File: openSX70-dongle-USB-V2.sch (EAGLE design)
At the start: 29 parts, among them J1 687106183722, J2 SJ-3523-SMT-TR, U1 FT232RLSSOP

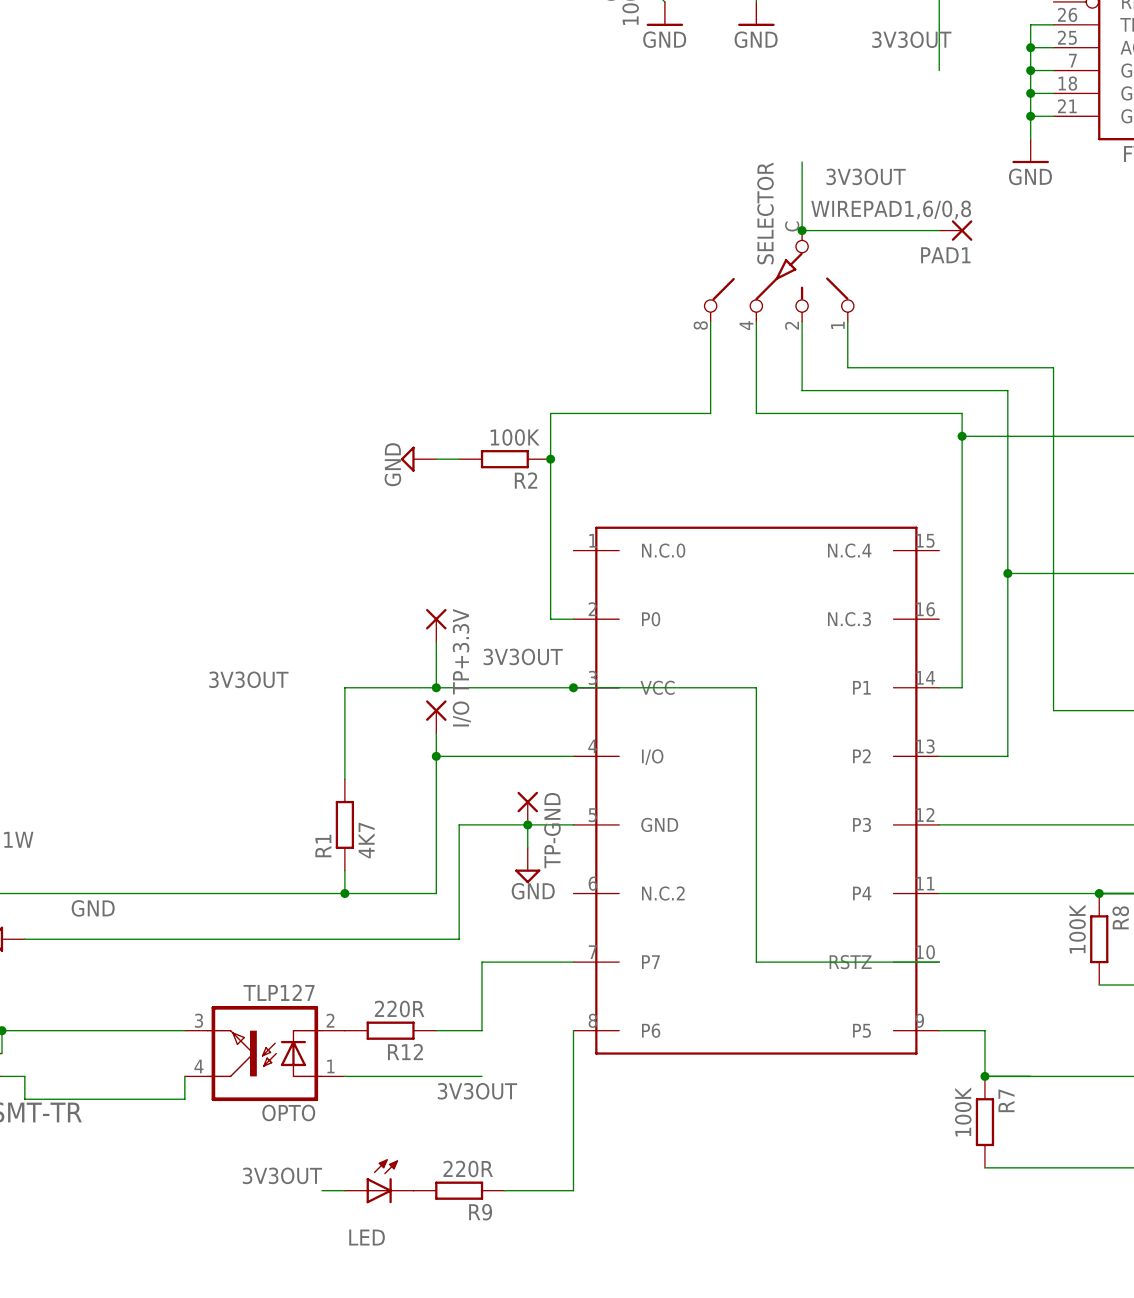
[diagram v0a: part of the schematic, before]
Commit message: new design, new parts
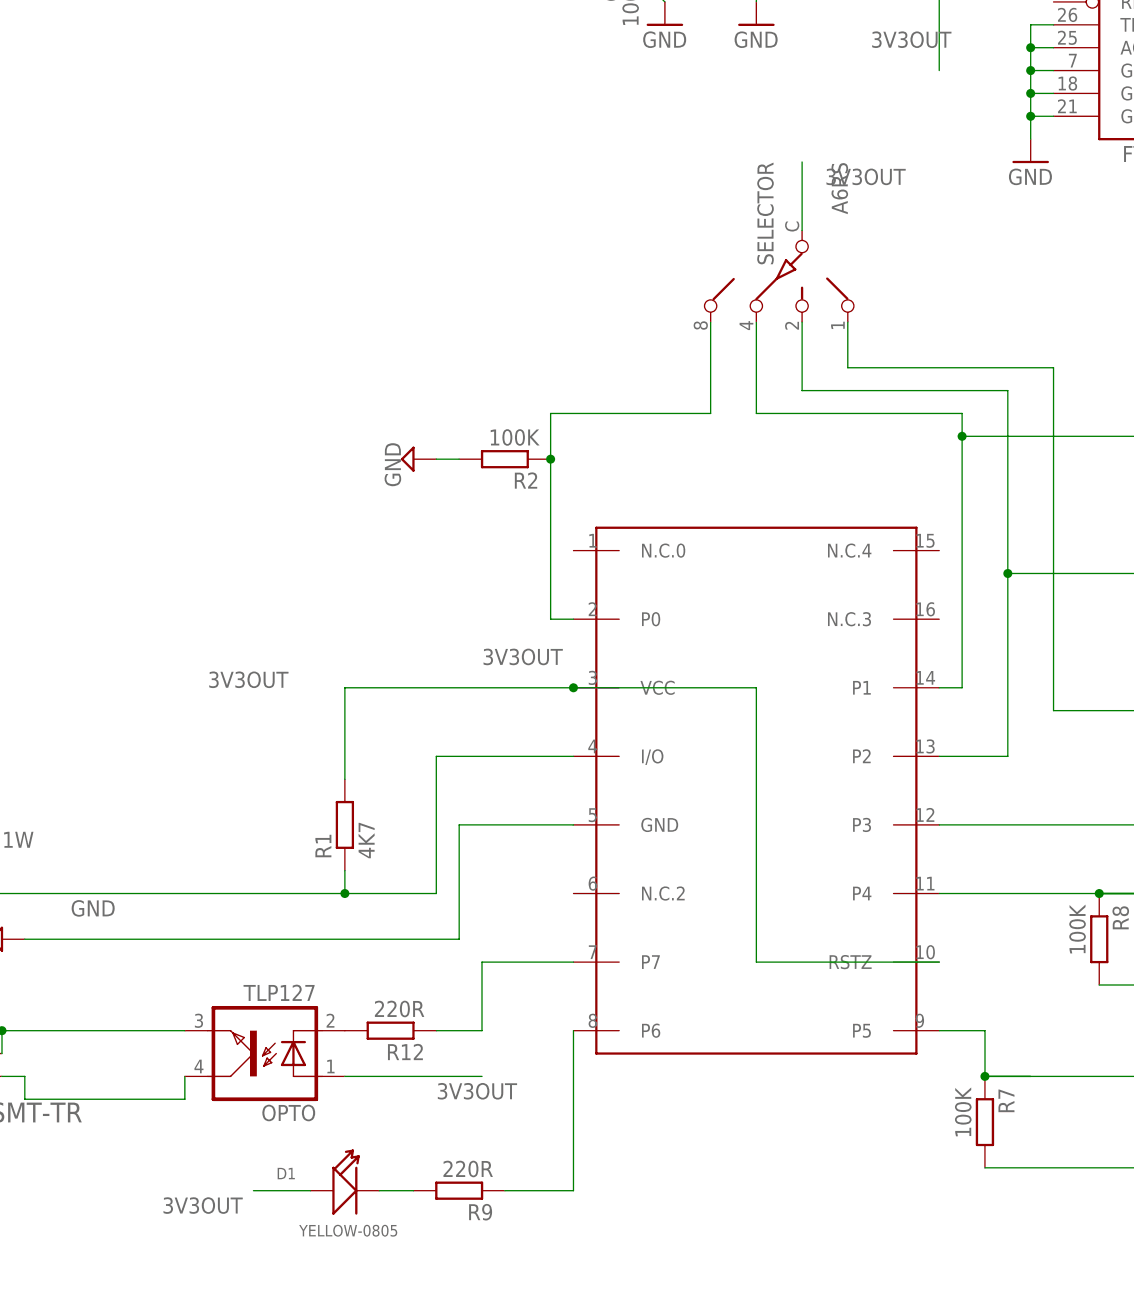
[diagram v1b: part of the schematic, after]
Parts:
- removed I/O, TP+3.3V, TP-GND: (no value), wirepad:SMD2
- removed LED: (no value), adafruit:LED3MM
- removed PAD1: WIREPAD1,6/0,8, wirepad:WIREPAD1,6/0,8
- added D1: YELLOW-0805, Seeed-LED-2016:SMD-LED-CLEAR-YELLOW(0805)
- SELECTOR: value (none) -> A6RS; device special:SW-C16 -> _openSX70:A6RS
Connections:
- net 1W: no longer I/O.P
- net 3V3OUT: now also D1.+; no longer LED.A, PAD1.P, TP+3.3V.P
- net GND: no longer TP-GND.P
- net N$2: now also D1.-; no longer LED.C
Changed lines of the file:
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@@
 <part name="R8" library="resistor" library_urn="urn:adsk.eagle:library:348" deviceset="R-EU_" device="R0603" package3d_urn="urn:adsk.eagle:package:26057/1" value="100K"/>
 <part name="R9" library="resistor" library_urn="urn:adsk.eagle:library:348" deviceset="R-EU_" device="R0603" package3d_urn="urn:adsk.eagle:package:26057/1" value="220R"/>
-<part name="SELECTOR" library="special" library_urn="urn:adsk.eagle:library:367" deviceset="SW-C16" device="" package3d_urn="urn:adsk.eagle:package:26665/1"/>
-<part name="GND-ISO1" library="supply2" library_urn="urn:adsk.eagle:library:372" deviceset="GND" device=""/>
+<part name="SELECTOR" library="_openSX70" deviceset="A6RS" device=""/>
 <part name="GND-ISO8" library="supply2" library_urn="urn:adsk.eagle:library:372" deviceset="GND" device=""/>
-<part name="LED" library="adafruit" library_urn="urn:adsk.eagle:library:420" deviceset="LED" device="3MM"/>
 <part name="OPTO" library="openSX70" deviceset="TLP127" device="" value="TLP127"/>
 <part name="R12" library="resistor" library_urn="urn:adsk.eagle:library:348" deviceset="R-EU_" device="R0603" package3d_urn="urn:adsk.eagle:package:26057/1" value="220R"/>
 <part name="FRAME1" library="frames" library_urn="urn:adsk.eagle:library:229" deviceset="DINA4_L" device=""/>
-<part name="TP+3.3V" library="wirepad" library_urn="urn:adsk.eagle:library:412" deviceset="SMD2" device="" package3d_urn="urn:adsk.eagle:package:30839/1"/>
-<part name="I/O" library="wirepad" library_urn="urn:adsk.eagle:library:412" deviceset="SMD2" device="" package3d_urn="urn:adsk.eagle:package:30839/1"/>
 <part name="GND-ISO6" library="supply2" library_urn="urn:adsk.eagle:library:372" deviceset="GND" device=""/>
 <part name="GND-ISO11" library="supply2" library_urn="urn:adsk.eagle:library:372" deviceset="GND" device=""/>
 <part name="GND-ISO12" library="supply2" library_urn="urn:adsk.eagle:library:372" deviceset="GND" device=""/>
-<part name="PAD1" library="wirepad" library_urn="urn:adsk.eagle:library:412" deviceset="WIREPAD" device="1,6/0,8" package3d_urn="urn:adsk.eagle:package:30830/1"/>
 <part name="C3" library="resistor" library_urn="urn:adsk.eagle:library:348" deviceset="C-EU" device="C0603" package3d_urn="urn:adsk.eagle:package:26138/1" value="100nf"/>
 <part name="C4" library="Seeed-Capacitor-2016" deviceset="TANTALUM-SMD-10UF-16V-10%(AVX-A)" device="" value="10uf"/>
@@
 <part name="S2" library="SparkFun-Switches" library_urn="urn:adsk.eagle:library:535" deviceset="SWITCH-SPDT" device="-SMD-RIGHT-ANGLE" package3d_urn="urn:adsk.eagle:package:40179/1"/>
 <part name="S3" library="SparkFun-Switches" library_urn="urn:adsk.eagle:library:535" deviceset="SWITCH-SPDT" device="-SMD-RIGHT-ANGLE" package3d_urn="urn:adsk.eagle:package:40179/1"/>
-<part name="TP-GND" library="wirepad" library_urn="urn:adsk.eagle:library:412" deviceset="SMD2" device="" package3d_urn="urn:adsk.eagle:package:30839/1"/>
 <part name="J2" library="SJ-3523-SMT-TR" deviceset="SJ-3523-SMT-TR" device=""/>
+<part name="D1" library="Seeed-LED-2016" deviceset="SMD-LED-CLEAR-YELLOW(0805)" device="" value="YELLOW-0805"/>
 </parts>
 <sheets>
@@
 <attribute name="VALUE" x="101.6" y="111.76" size="1.778" layer="96" rot="MR270"/>
 </instance>
-<instance part="GND-ISO1" gate="GND" x="66.04" y="33.02">
-<attribute name="VALUE" x="64.135" y="29.845" size="1.778" layer="96"/>
-</instance>
 <instance part="GND-ISO8" gate="GND" x="149.86" y="20.32" rot="R90">
 <attribute name="VALUE" x="153.035" y="18.415" size="1.778" layer="96" rot="R90"/>
-</instance>
-<instance part="LED" gate="G$1" x="48.26" y="-2.54" rot="MR270">
-<attribute name="NAME" x="50.292" y="-8.636" size="1.778" layer="95" rot="MR0"/>
-<attribute name="VALUE" x="52.832" y="-8.255" size="1.778" layer="96" rot="MR0"/>
 </instance>
 <instance part="OPTO" gate="G$1" x="35.56" y="12.7" rot="R180">
@@
 <attribute name="DRAWING_NAME" x="172.72" y="3.81" size="2.54" layer="94"/>
 </instance>
-<instance part="TP+3.3V" gate="1" x="55.88" y="60.96" rot="R270">
-<attribute name="NAME" x="57.7342" y="62.103" size="1.778" layer="95" rot="R270"/>
-<attribute name="VALUE" x="52.578" y="62.103" size="1.778" layer="96" rot="R270"/>
-</instance>
-<instance part="I/O" gate="1" x="55.88" y="50.8" rot="R270">
-<attribute name="NAME" x="57.7342" y="51.943" size="1.778" layer="95" rot="R270"/>
-<attribute name="VALUE" x="52.578" y="51.943" size="1.778" layer="96" rot="R270"/>
-</instance>
 <instance part="GND-ISO6" gate="GND" x="149.86" y="0" rot="R90">
 <attribute name="VALUE" x="153.035" y="-1.905" size="1.778" layer="96" rot="R90"/>
@@
 <instance part="GND-ISO12" gate="GND" x="185.42" y="66.04" rot="R90">
 <attribute name="VALUE" x="188.595" y="64.135" size="1.778" layer="96" rot="R90"/>
-</instance>
-<instance part="PAD1" gate="G$1" x="114.3" y="104.14" rot="R180">
-<attribute name="NAME" x="115.443" y="102.2858" size="1.778" layer="95" rot="R180"/>
-<attribute name="VALUE" x="115.443" y="107.442" size="1.778" layer="96" rot="R180"/>
 </instance>
 <instance part="C3" gate="G$1" x="81.28" y="134.62" rot="R270">
@@
 <attribute name="VALUE" x="138.176" y="6.858" size="1.778" layer="96" font="vector" align="top-center"/>
 </instance>
-<instance part="TP-GND" gate="1" x="66.04" y="40.64" rot="R270">
-<attribute name="NAME" x="67.8942" y="41.783" size="1.778" layer="95" rot="R270"/>
-<attribute name="VALUE" x="62.738" y="41.783" size="1.778" layer="96" rot="R270"/>
-</instance>
 <instance part="J2" gate="G$1" x="0" y="12.7">
 <attribute name="NAME" x="-5.100409375" y="18.437959375" size="2.201440625" layer="95"/>
 <attribute name="VALUE" x="-5.10061875" y="5.04906875" size="2.20203125" layer="96"/>
+</instance>
+<instance part="D1" gate="G$1" x="45.72" y="-2.54">
+<attribute name="NAME" x="38.1" y="-1.27" size="1.27" layer="95" ratio="10"/>
+<attribute name="VALUE" x="40.64" y="-7.62" size="1.27" layer="96" ratio="10"/>
 </instance>
 </instances>
@@
 <wire x1="45.72" y1="33.02" x2="45.72" y2="30.48" width="0.1524" layer="91"/>
 <junction x="45.72" y="30.48"/>
-<pinref part="I/O" gate="1" pin="P"/>
-<wire x1="55.88" y1="48.26" x2="55.88" y2="45.72" width="0.1524" layer="91"/>
-<junction x="55.88" y="45.72"/>
 <label x="7.62" y="35.56" size="1.778" layer="95"/>
 </segment>
@@
 <segment>
 <pinref part="DS2408" gate="G$1" pin="GND"/>
-<wire x1="58.42" y1="38.1" x2="66.04" y2="38.1" width="0.1524" layer="91"/>
-<wire x1="66.04" y1="38.1" x2="71.12" y2="38.1" width="0.1524" layer="91"/>
+<wire x1="58.42" y1="38.1" x2="71.12" y2="38.1" width="0.1524" layer="91"/>
 <wire x1="58.42" y1="25.4" x2="58.42" y2="38.1" width="0.1524" layer="91"/>
-<pinref part="GND-ISO1" gate="GND" pin="GND"/>
 <wire x1="10.16" y1="25.4" x2="58.42" y2="25.4" width="0.1524" layer="91"/>
-<wire x1="66.04" y1="35.56" x2="66.04" y2="38.1" width="0.1524" layer="91"/>
-<junction x="66.04" y="38.1"/>
 <label x="15.24" y="27.94" size="1.778" layer="95"/>
 <pinref part="GND-ISO2" gate="GND" pin="GND"/>
-<pinref part="TP-GND" gate="1" pin="P"/>
 </segment>
 <segment>
@@
 </segment>
 </net>
-<net name="N$2" class="0">
-<segment>
-<pinref part="LED" gate="G$1" pin="C"/>
-<pinref part="R9" gate="G$1" pin="2"/>
-</segment>
-</net>
 <net name="N$8" class="0">
 <segment>
@@
 <wire x1="91.44" y1="22.86" x2="111.76" y2="22.86" width="0.1524" layer="91"/>
 <junction x="71.12" y="53.34"/>
-<pinref part="TP+3.3V" gate="1" pin="P"/>
-<wire x1="55.88" y1="53.34" x2="71.12" y2="53.34" width="0.1524" layer="91"/>
-<wire x1="55.88" y1="58.42" x2="55.88" y2="53.34" width="0.1524" layer="91"/>
-<wire x1="45.72" y1="53.34" x2="55.88" y2="53.34" width="0.1524" layer="91"/>
-<junction x="55.88" y="53.34"/>
+<wire x1="45.72" y1="53.34" x2="71.12" y2="53.34" width="0.1524" layer="91"/>
 <label x="60.96" y="55.88" size="1.778" layer="95"/>
 </segment>
@@
 <wire x1="96.52" y1="111.76" x2="96.52" y2="104.14" width="0.1524" layer="91"/>
 <label x="99.06" y="109.22" size="1.778" layer="95"/>
-<junction x="96.52" y="104.14"/>
-<pinref part="PAD1" gate="G$1" pin="P"/>
-<wire x1="111.76" y1="104.14" x2="96.52" y2="104.14" width="0.1524" layer="91"/>
 </segment>
 <segment>
@@
 </segment>
 <segment>
-<pinref part="LED" gate="G$1" pin="A"/>
-<wire x1="43.18" y1="-2.54" x2="45.72" y2="-2.54" width="0.1524" layer="91"/>
-<label x="43.18" y="0" size="1.778" layer="95" rot="R180"/>
-</segment>
-<segment>
 <pinref part="S3" gate="1" pin="O"/>
 <wire x1="142.24" y1="12.7" x2="149.86" y2="12.7" width="0.1524" layer="91"/>
 <label x="142.24" y="15.24" size="1.778" layer="95"/>
+</segment>
+<segment>
+<pinref part="D1" gate="G$1" pin="+"/>
+<wire x1="41.91" y1="-2.54" x2="35.56" y2="-2.54" width="0.1524" layer="91"/>
+<label x="25.4" y="-5.08" size="1.778" layer="95"/>
 </segment>
 </net>
@@
 </segment>
 </net>
+<net name="N$2" class="0">
+<segment>
+<pinref part="D1" gate="G$1" pin="-"/>
+<pinref part="R9" gate="G$1" pin="2"/>
+<wire x1="49.53" y1="-2.54" x2="53.34" y2="-2.54" width="0.1524" layer="91"/>
+</segment>
+</net>
